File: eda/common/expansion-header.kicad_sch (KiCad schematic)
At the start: 10 parts, among them J2 Bus expansion

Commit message: Sync
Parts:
- removed J2: Bus expansion, Connector_PinHeader_2.54mm:PinHeader_2x20_P2.54mm_Horizontal, symbol Connector_Generic:Conn_02x20_Odd_Even
- added J2: Conn_02x25_Odd_Even, Connector_PinHeader_2.54mm:PinHeader_2x25_P2.54mm_Horizontal, symbol Connector_Generic:Conn_02x25_Odd_Even
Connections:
- net A0: now also J2.5 (Pin_5)
- net A1: now also J2.7 (Pin_7)
- net A10: now also J2.25 (Pin_25)
- net A11: now also J2.27 (Pin_27)
- net A12: now also J2.29 (Pin_29)
- net A13: now also J2.31 (Pin_31)
- net A14: now also J2.33 (Pin_33)
- net A15: now also J2.35 (Pin_35)
- net A2: now also J2.9 (Pin_9)
- net A3: now also J2.11 (Pin_11)
- net A4: now also J2.13 (Pin_13)
- net A5: now also J2.15 (Pin_15)
- net A6: now also J2.17 (Pin_17)
- net A7: now also J2.19 (Pin_19)
- net A8: now also J2.21 (Pin_21)
- net A9: now also J2.23 (Pin_23)
- net Clock: now also J2.39 (Pin_39)
- net D0: now also J2.4 (Pin_4)
- net D1: now also J2.6 (Pin_6)
- net D2: now also J2.8 (Pin_8)
- net D3: now also J2.10 (Pin_10)
- net D4: now also J2.12 (Pin_12)
- net D5: now also J2.14 (Pin_14)
- net D6: now also J2.16 (Pin_16)
- net D7: now also J2.18 (Pin_18)
- net GND: now also J2.2 (Pin_2), J2.20 (Pin_20), J2.3 (Pin_3), J2.37 (Pin_37), J2.38 (Pin_38), J2.45 (Pin_45), J2.46 (Pin_46)
- net R~{W}: now also J2.41 (Pin_41)
- net VCC: now also J2.1 (Pin_1)
- net ~{DMA}: now also J2.43 (Pin_43)
- net ~{IRQ}: now also J2.44 (Pin_44)
- net ~{NMI}: now also J2.42 (Pin_42)
- net ~{RST}: now also J2.40 (Pin_40)
- net at JP1.1 (A): now also J2.22 (Pin_22)
- net at JP2.1 (A): now also J2.24 (Pin_24)
- net at JP3.1 (A): now also J2.26 (Pin_26)
- net at JP4.1 (A): now also J2.28 (Pin_28)
- net at JP5.1 (A): now also J2.30 (Pin_30)
- net at JP6.1 (A): now also J2.32 (Pin_32)
- net at JP7.1 (A): now also J2.34 (Pin_34)
- net at JP8.1 (A): now also J2.36 (Pin_36)

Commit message: EDA work for new expansion header
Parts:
- J2: footprint Connector_PinHeader_2.54mm:PinHeader_2x25_P2.54mm_Horizontal -> Connector_PinHeader_2.54mm:PinHeader_2x25_P2.54mm_Vertical
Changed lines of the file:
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@@
       (effects (font (size 1.27 1.27)))
     )
-    (property "Footprint" "Connector_PinHeader_2.54mm:PinHeader_2x25_P2.54mm_Horizontal" (at 154.94 79.502 0)
+    (property "Footprint" "Connector_PinHeader_2.54mm:PinHeader_2x25_P2.54mm_Vertical" (at 154.94 79.502 0)
       (effects (font (size 1.27 1.27)) hide)
     )
@@
           (reference "J2") (unit 1)
         )
+      )
+      (project "io-card"
+        (path "/88a1e5ee-bcfe-4f55-a7a9-4b7b5eaf475b/5d80791e-4732-481b-8542-898a0c887aef"
+          (reference "J2") (unit 1)
+        )

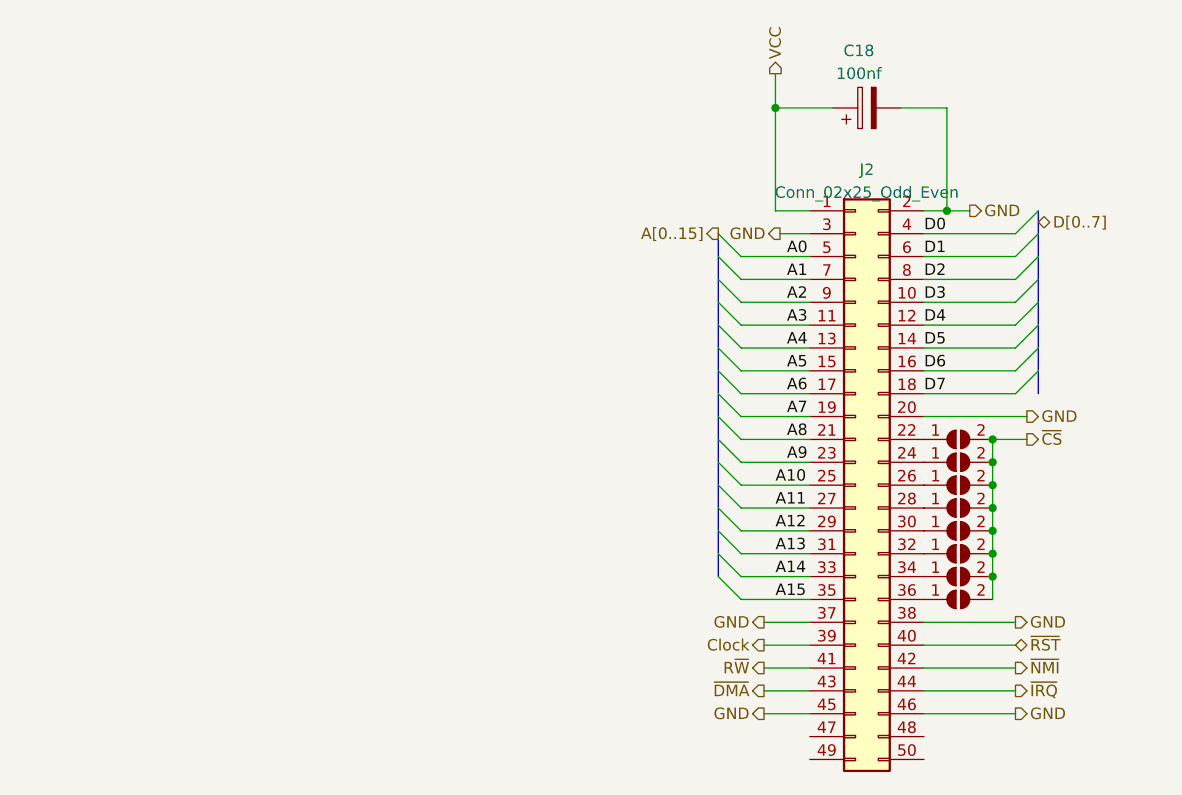
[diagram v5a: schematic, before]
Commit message: Add conversion board
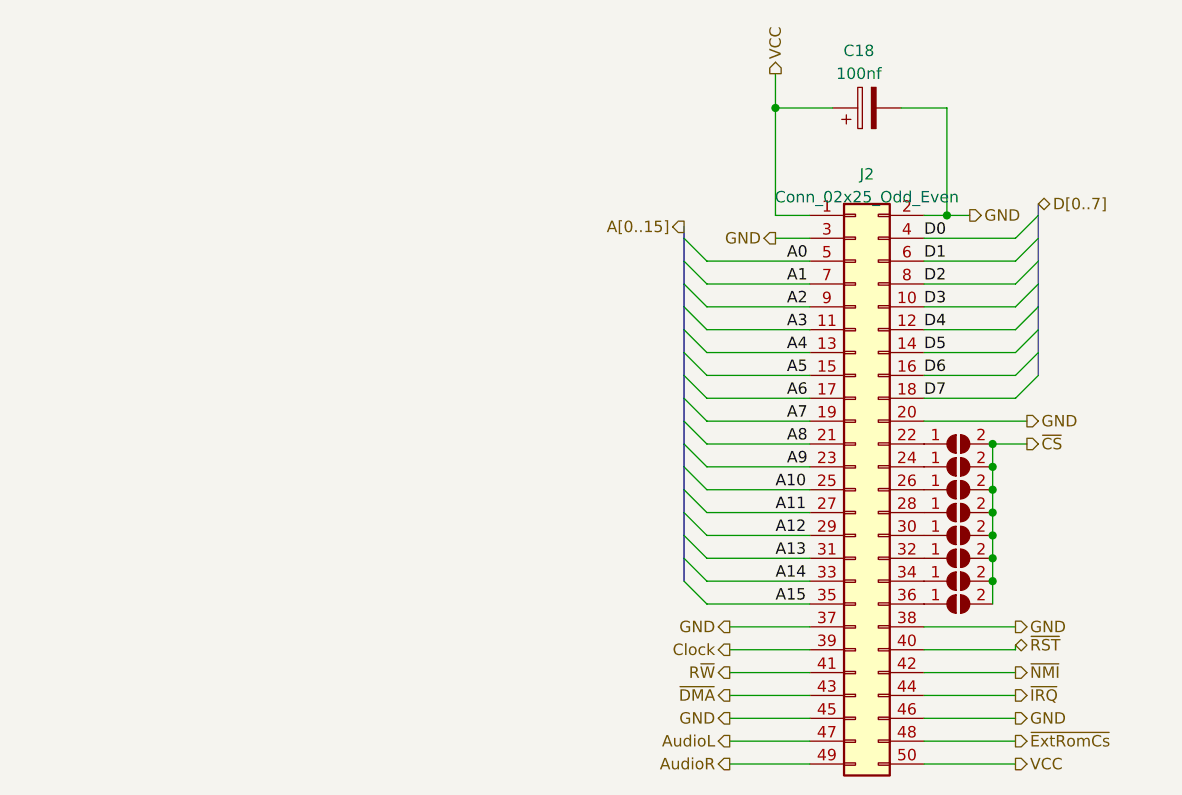
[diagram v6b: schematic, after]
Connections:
- net VCC: now also J2.50 (Pin_50)
- net AudioL: now reaches J2.47 (Pin_47)
- net ~{ExtRomCs}: now reaches J2.48 (Pin_48)
- net AudioR: now reaches J2.49 (Pin_49)
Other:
- moved on the sheet: J2

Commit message: Add SPI
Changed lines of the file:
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@@
 (kicad_sch
-	(version 20231120)
+	(version 20250114)
 	(generator "eeschema")
-	(generator_version "8.0")
+	(generator_version "9.0")
 	(paper "A4")
 	(junction
@@
 	(label "A6"
 		(at 147.32 69.85 0)
-		(fields_autoplaced yes)
 		(effects
 			(font
@@
 	(label "A13"
 		(at 146.05 87.63 0)
-		(fields_autoplaced yes)
 		(effects
 			(font
@@
 	(label "D1"
 		(at 162.56 54.61 0)
-		(fields_autoplaced yes)
 		(effects
 			(font
@@
 	(label "A7"
 		(at 147.32 72.39 0)
-		(fields_autoplaced yes)
 		(effects
 			(font
@@
 	(label "A2"
 		(at 147.32 59.69 0)
-		(fields_autoplaced yes)
 		(effects
 			(font
@@
 	(label "A14"
 		(at 146.05 90.17 0)
-		(fields_autoplaced yes)
 		(effects
 			(font
@@
 	(label "A15"
 		(at 146.05 92.71 0)
-		(fields_autoplaced yes)
 		(effects
 			(font
@@
 	(label "A9"
 		(at 147.32 77.47 0)
-		(fields_autoplaced yes)
 		(effects
 			(font
@@
 	(label "A0"
 		(at 147.32 54.61 0)
-		(fields_autoplaced yes)
 		(effects
 			(font
@@
 	(label "D4"
 		(at 162.56 62.23 0)
-		(fields_autoplaced yes)
 		(effects
 			(font
@@
 	(label "A11"
 		(at 146.05 82.55 0)
-		(fields_autoplaced yes)
 		(effects
 			(font
@@
 	(label "A10"
 		(at 146.05 80.01 0)
-		(fields_autoplaced yes)
 		(effects
 			(font
@@
 	(label "A4"
 		(at 147.32 64.77 0)
-		(fields_autoplaced yes)
 		(effects
 			(font
@@
 	(label "D7"
 		(at 162.56 69.85 0)
-		(fields_autoplaced yes)
 		(effects
 			(font
@@
 	(label "A12"
 		(at 146.05 85.09 0)
-		(fields_autoplaced yes)
 		(effects
 			(font
@@
 	(label "A8"
 		(at 147.32 74.93 0)
-		(fields_autoplaced yes)
 		(effects
 			(font
@@
 	(label "A5"
 		(at 147.32 67.31 0)
-		(fields_autoplaced yes)
 		(effects
 			(font
@@
 	(label "D5"
 		(at 162.56 64.77 0)
-		(fields_autoplaced yes)
 		(effects
 			(font
@@
 	(label "A1"
 		(at 147.32 57.15 0)
-		(fields_autoplaced yes)
 		(effects
 			(font
@@
 	(label "D3"
 		(at 162.56 59.69 0)
-		(fields_autoplaced yes)
 		(effects
 			(font
@@
 	(label "D6"
 		(at 162.56 67.31 0)
-		(fields_autoplaced yes)
 		(effects
 			(font
@@
 	(label "A3"
 		(at 147.32 62.23 0)
-		(fields_autoplaced yes)
 		(effects
 			(font
@@
 	(label "D2"
 		(at 162.56 57.15 0)
-		(fields_autoplaced yes)
 		(effects
 			(font
@@
 	(label "D0"
 		(at 162.56 52.07 0)
-		(fields_autoplaced yes)
 		(effects
 			(font
@@
 		(shape output)
 		(at 140.97 97.79 180)
-		(fields_autoplaced yes)
 		(effects
 			(font
@@
 		(shape output)
 		(at 146.05 52.07 180)
-		(fields_autoplaced yes)
 		(effects
 			(font
@@
 		(shape output)
 		(at 172.72 102.87 0)
-		(fields_autoplaced yes)
 		(effects
 			(font
@@
 		(shape output)
 		(at 172.72 110.49 0)
-		(fields_autoplaced yes)
 		(effects
 			(font
@@
 		(shape output)
 		(at 140.97 102.87 180)
-		(fields_autoplaced yes)
 		(effects
 			(font
@@
 		(shape output)
 		(at 140.97 110.49 180)
-		(fields_autoplaced yes)
 		(effects
 			(font
@@
 		(shape output)
 		(at 140.97 107.95 180)
-		(fields_autoplaced yes)
 		(effects
 			(font
@@
 		(shape output)
 		(at 172.72 95.25 0)
-		(fields_autoplaced yes)
 		(effects
 			(font
@@
 		(shape output)
 		(at 146.05 33.782 90)
-		(fields_autoplaced yes)
 		(effects
 			(font
@@
 		(shape output)
 		(at 172.72 105.41 0)
-		(fields_autoplaced yes)
 		(effects
 			(font
@@
 		(shape output)
 		(at 173.99 72.39 0)
-		(fields_autoplaced yes)
 		(effects
 			(font
@@
 		(shape output)
 		(at 173.99 74.93 0)
-		(fields_autoplaced yes)
 		(effects
 			(font
@@
 		(shape output)
 		(at 140.97 95.25 180)
-		(fields_autoplaced yes)
 		(effects
 			(font
@@
 		(shape output)
 		(at 140.97 100.33 180)
-		(fields_autoplaced yes)
 		(effects
 			(font
@@
 		(shape bidirectional)
 		(at 172.72 97.282 0)
-		(fields_autoplaced yes)
 		(effects
 			(font
@@
 		(shape output)
 		(at 172.72 100.33 0)
-		(fields_autoplaced yes)
 		(effects
 			(font
@@
 		(shape output)
 		(at 172.72 107.95 0)
-		(fields_autoplaced yes)
 		(effects
 			(font
@@
 		(shape output)
 		(at 140.97 105.41 180)
-		(fields_autoplaced yes)
 		(effects
 			(font
@@
 		(shape output)
 		(at 167.64 49.53 0)
-		(fields_autoplaced yes)
 		(effects
 			(font
@@
 		(shape output)
 		(at 135.89 50.8 180)
-		(fields_autoplaced yes)
 		(effects
 			(font
@@
 		(shape tri_state)
 		(at 175.26 48.26 0)
-		(fields_autoplaced yes)
 		(effects
 			(font
@@
 		)
 	)
+	(embedded_fonts no)
 )
